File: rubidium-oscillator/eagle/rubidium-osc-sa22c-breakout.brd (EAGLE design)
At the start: 58.9 x 66 mm, 12 parts, among them J1 OSC_TMMH-109-01-G-DV-ES-A, Q1 ZXMP10A13F, Q2 ZXMP10A13F, X1 MKDSN4, X2 MPT9, X3 SMA-142-0701-801/806, X4 SMA-142-0701-801/806, X5 SMA-142-0701-801/806

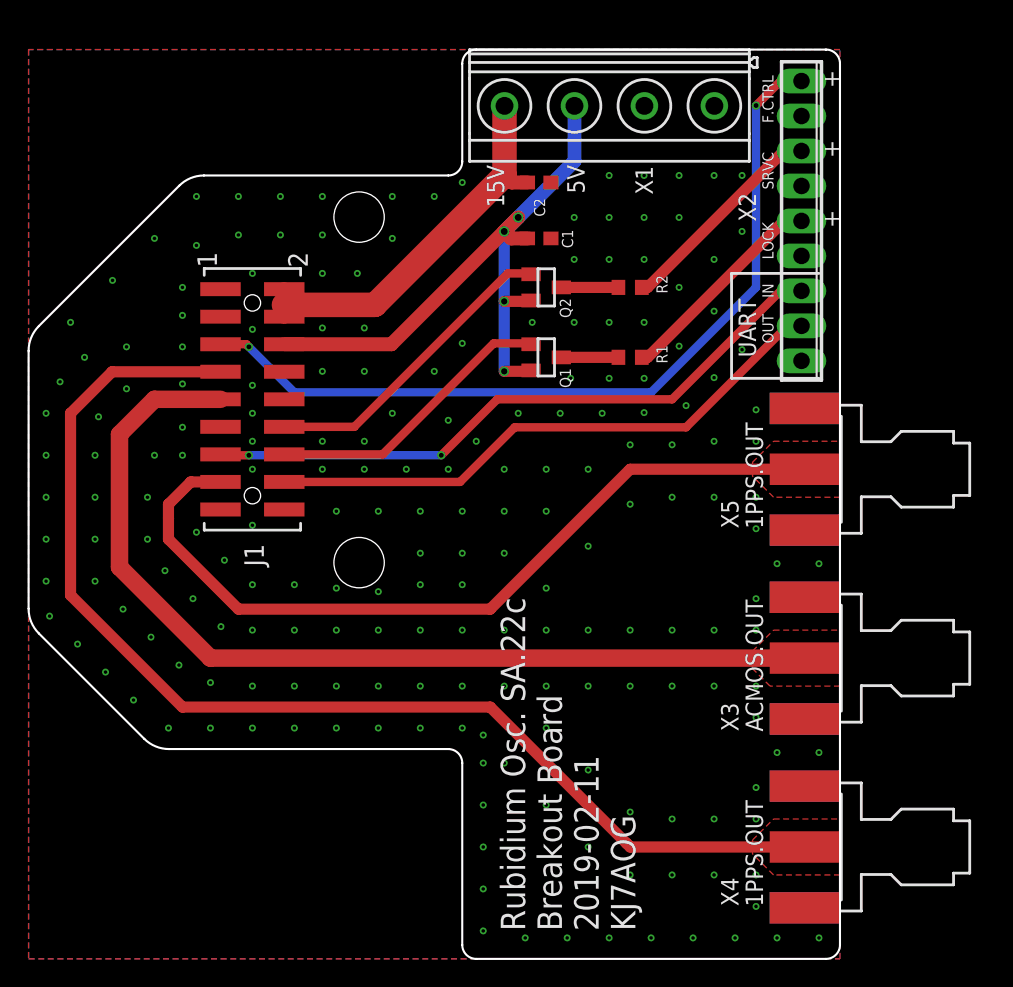
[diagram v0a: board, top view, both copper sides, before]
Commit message: Adjust for proper Phoenix conn sizes.
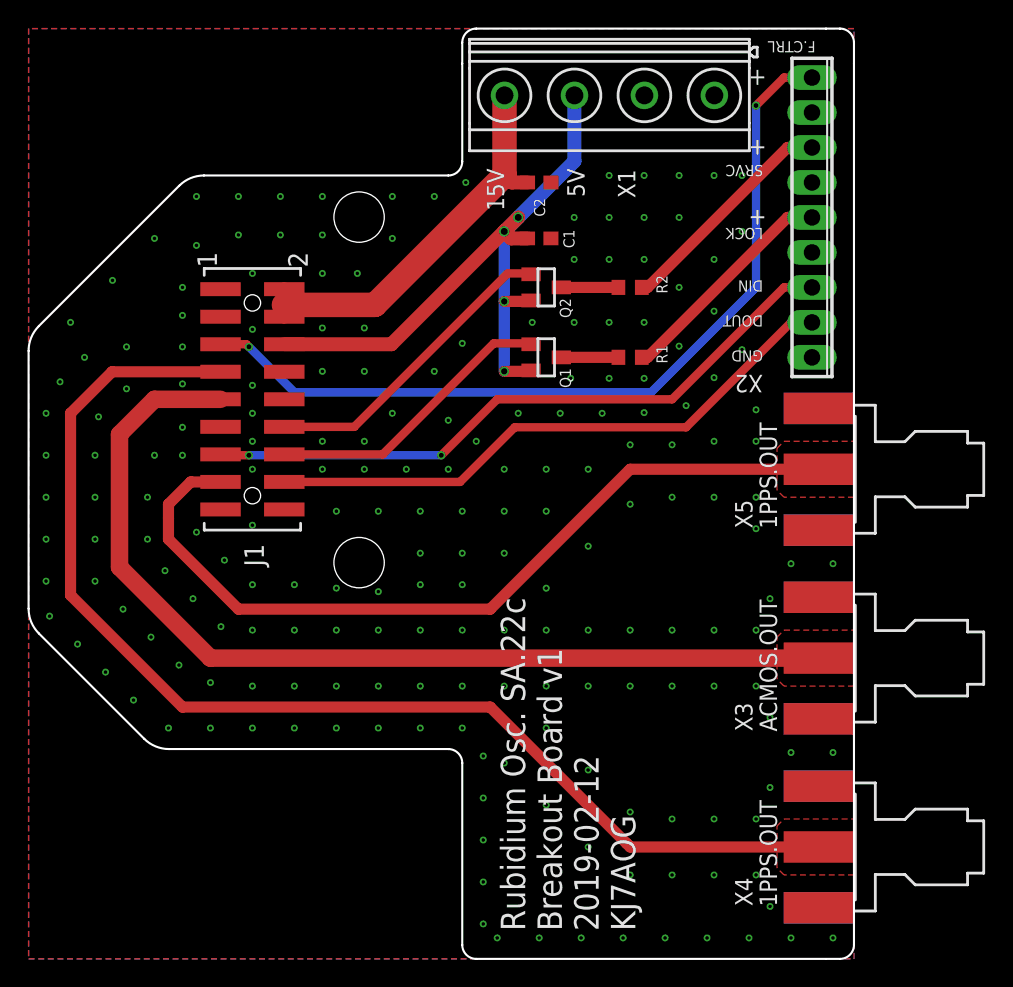
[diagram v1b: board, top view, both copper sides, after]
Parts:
- moved X3 1.02 mm to (59.9, 21.8)
- moved X4 1.02 mm to (59.9, 8.13)
- moved X5 1.02 mm to (59.9, 35.6)
- moved X2 0.80 mm to (56.9, 53.8)
- moved X1 0.76 mm to (42.2, 62.7)
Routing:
- net N$3: track 59.5 -> 60.5 mm
- net N$2: track 86.2 -> 87.3 mm
- net N$1: track 70.5 -> 71.6 mm
- net N$7: track 60.7 -> 61.6 mm
- net N$5: track 42.3 -> 43.1 mm
- net N$4: track 47.2 -> 48.0 mm
- net N$13: track 15.7 -> 16.6 mm
- net N$12: track 15.7 -> 16.6 mm
- net +5V: track 48.0 -> 48.8 mm
- net +15V: track 28.9 -> 29.6 mm
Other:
- board size 58.9 x 66 mm -> 59.9 x 67.6 mm
- board text added: "DIN"
- board text added: "DOUT"
- board text added: "GND"
- board text added: "Rubidium Osc. SA.22c Breakout Board v1 2019-02-12 KJ7AOG"
- board text removed: "IN"
- board text removed: "OUT"
- board text removed: "Rubidium Osc. SA.22c Breakout Board 2019-02-11 KJ7AOG"
- board text removed: "UART"

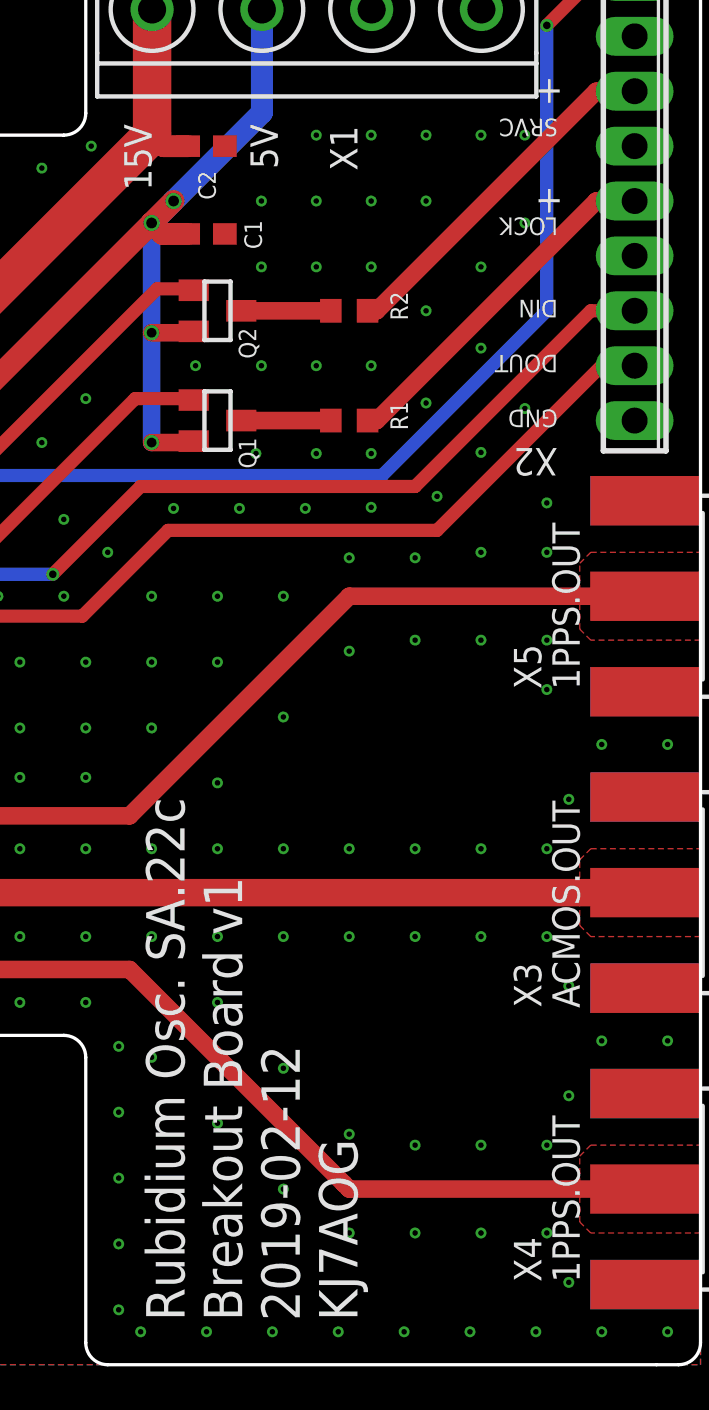
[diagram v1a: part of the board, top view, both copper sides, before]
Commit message: Update vias to tented and moved some, change R1 and R2 for 10mA LEDs
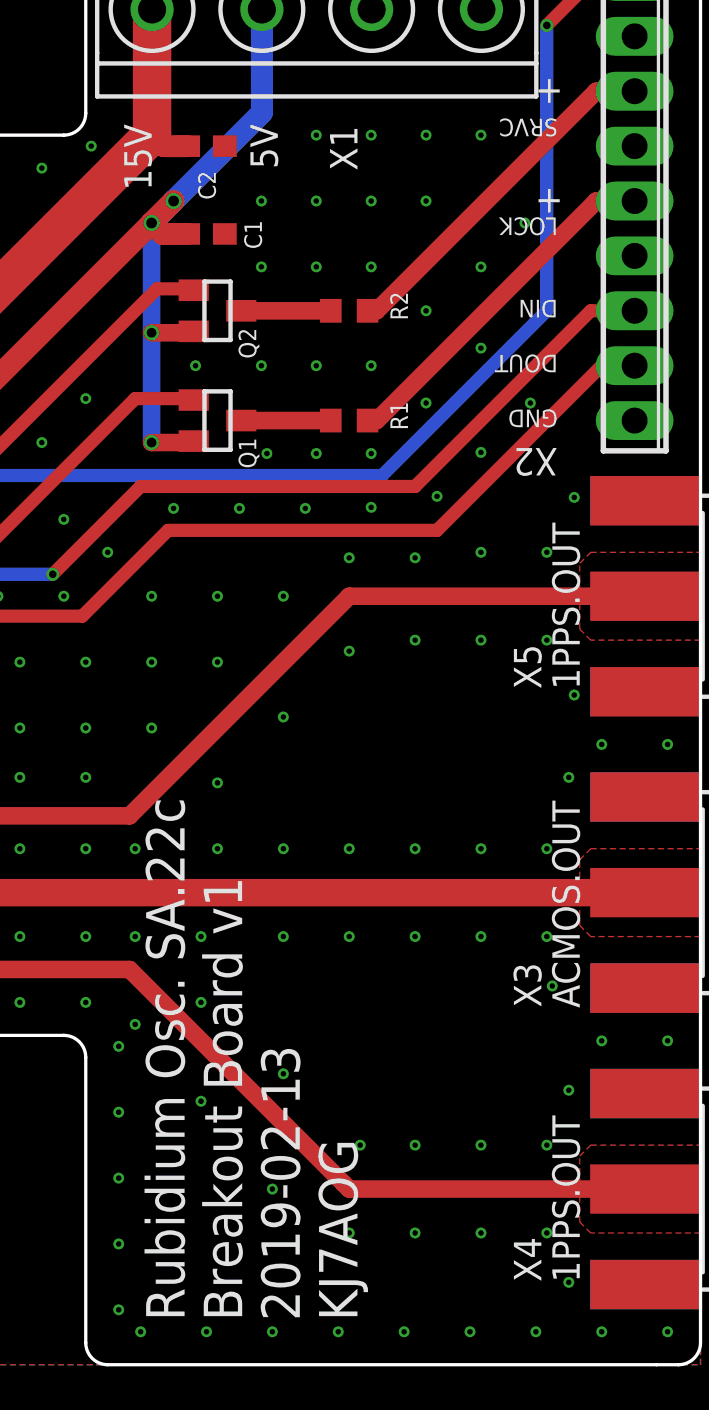
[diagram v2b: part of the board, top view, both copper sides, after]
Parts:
- R1: value 560 -> 270
- R2: value 1k -> 270
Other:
- board text added: "Rubidium Osc. SA.22c Breakout Board v1 2019-02-13 KJ7AOG"
- board text removed: "Rubidium Osc. SA.22c Breakout Board v1 2019-02-12 KJ7AOG"
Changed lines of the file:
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@@
 <layer number="27" name="tValues" color="7" fill="1" visible="yes" active="yes"/>
 <layer number="28" name="bValues" color="7" fill="1" visible="yes" active="yes"/>
-<layer number="29" name="tStop" color="7" fill="3" visible="no" active="yes"/>
+<layer number="29" name="tStop" color="7" fill="3" visible="yes" active="yes"/>
 <layer number="30" name="bStop" color="7" fill="6" visible="no" active="yes"/>
 <layer number="31" name="tCream" color="7" fill="4" visible="no" active="yes"/>
@@
 <text x="34.29" y="2.032" size="1.778" layer="21" ratio="10" rot="R90" align="top-left">Rubidium Osc. SA.22c
 Breakout Board v1
-2019-02-12
+2019-02-13
 KJ7AOG</text>
 <wire x1="53.848" y1="65.024" x2="59.944" y2="65.024" width="0.1524" layer="51"/>
@@
 </class>
 </classes>
-<designrules name="oshpark-2layer">
+<designrules name="oshpark-2layer-tented">
 <description language="en">&lt;b&gt;OSH Park Design Rules&lt;/b&gt;
 &lt;p&gt;
 Please make sure your boards conform to these design rules.
+&lt;/p&gt;
+&lt;p&gt;
+This DRC tents small vias, making them inaccessible on the produced board. This is great for dense routing, BGA, or production boards.
 &lt;/p&gt;
 &lt;p&gt;
@@
 <param name="mlMinCreamFrame" value="0mil"/>
 <param name="mlMaxCreamFrame" value="0mil"/>
-<param name="mlViaStopLimit" value="0mil"/>
+<param name="mlViaStopLimit" value="20mil"/>
 <param name="srRoundness" value="0"/>
 <param name="srMinRoundness" value="0mil"/>
@@
 <attribute name="NAME" x="38.576" y="47.978" size="0.8128" layer="25" rot="R270"/>
 </element>
-<element name="R1" library="rcl" library_urn="urn:adsk.eagle:library:334" package="R0603" package3d_urn="urn:adsk.eagle:package:23555/3" value="560" x="43.688" y="43.688" smashed="yes" rot="R180">
+<element name="R1" library="rcl" library_urn="urn:adsk.eagle:library:334" package="R0603" package3d_urn="urn:adsk.eagle:package:23555/3" value="270" x="43.688" y="43.688" smashed="yes" rot="R180">
 <attribute name="NAME" x="45.593" y="44.577" size="0.8128" layer="25" rot="R270"/>
 <attribute name="SPICEPREFIX" value="R" x="20.828" y="122.428" size="1.778" layer="27" rot="R180" display="off"/>
 </element>
-<element name="R2" library="rcl" library_urn="urn:adsk.eagle:library:334" package="R0603" package3d_urn="urn:adsk.eagle:package:23555/3" value="1k" x="43.688" y="48.768" smashed="yes" rot="R180">
+<element name="R2" library="rcl" library_urn="urn:adsk.eagle:library:334" package="R0603" package3d_urn="urn:adsk.eagle:package:23555/3" value="270" x="43.688" y="48.768" smashed="yes" rot="R180">
 <attribute name="NAME" x="45.593" y="49.657" size="0.8128" layer="25" rot="R270"/>
 <attribute name="SPICEPREFIX" value="R" x="17.018" y="127.508" size="1.778" layer="27" rot="R180" display="off"/>
@@
 <via x="47.244" y="48.768" extent="1-16" drill="0.254"/>
 <via x="49.784" y="50.8" extent="1-16" drill="0.254"/>
-<via x="39.37" y="42.164" extent="1-16" drill="0.254"/>
+<via x="39.878" y="42.164" extent="1-16" drill="0.254"/>
 <via x="42.164" y="42.164" extent="1-16" drill="0.254"/>
 <via x="44.704" y="42.164" extent="1-16" drill="0.254"/>
 <via x="47.244" y="44.5008" extent="1-16" drill="0.254"/>
 <via x="49.784" y="47.0408" extent="1-16" drill="0.254"/>
-<via x="51.816" y="56.896" extent="1-16" drill="0.254"/>
 <via x="51.816" y="52.832" extent="1-16" drill="0.254"/>
 <via x="49.784" y="42.2148" extent="1-16" drill="0.254"/>
-<via x="51.816" y="44.2468" extent="1-16" drill="0.254"/>
+<via x="52.07" y="44.5008" extent="1-16" drill="0.254"/>
 <via x="47.752" y="40.1828" extent="1-16" drill="0.254"/>
 <via x="44.704" y="39.6748" extent="1-16" drill="0.254"/>
@@
 <via x="27.432" y="35.56" extent="1-16" drill="0.254"/>
 <via x="32.512" y="37.592" extent="1-16" drill="0.254"/>
-<via x="34.544" y="23.876" extent="1-16" drill="0.254"/>
+<via x="33.782" y="23.876" extent="1-16" drill="0.254"/>
 <via x="37.592" y="23.876" extent="1-16" drill="0.254"/>
 <via x="40.64" y="23.876" extent="1-16" drill="0.254"/>
 <via x="43.688" y="23.876" extent="1-16" drill="0.254"/>
 <via x="46.736" y="23.876" extent="1-16" drill="0.254"/>
-<via x="34.544" y="19.812" extent="1-16" drill="0.254"/>
-<via x="37.592" y="19.812" extent="1-16" drill="0.254"/>
+<via x="33.782" y="19.812" extent="1-16" drill="0.254"/>
+<via x="36.83" y="19.812" extent="1-16" drill="0.254"/>
 <via x="40.64" y="19.812" extent="1-16" drill="0.254"/>
 <via x="43.688" y="19.812" extent="1-16" drill="0.254"/>
@@
 <via x="49.784" y="19.812" extent="1-16" drill="0.254"/>
 <via x="49.784" y="23.876" extent="1-16" drill="0.254"/>
-<via x="53.848" y="17.526" extent="1-16" drill="0.254"/>
-<via x="53.848" y="26.162" extent="1-16" drill="0.254"/>
+<via x="53.086" y="17.526" extent="1-16" drill="0.254"/>
+<via x="53.848" y="27.178" extent="1-16" drill="0.254"/>
 <via x="52.832" y="23.876" extent="1-16" drill="0.254"/>
 <via x="52.832" y="19.812" extent="1-16" drill="0.254"/>
-<via x="53.848" y="12.446" extent="1-16" drill="0.254"/>
+<via x="53.848" y="12.7" extent="1-16" drill="0.254"/>
 <via x="53.848" y="3.81" extent="1-16" drill="0.254"/>
 <via x="52.832" y="10.16" extent="1-16" drill="0.254"/>
@@
 <via x="49.784" y="10.16" extent="1-16" drill="0.254"/>
 <via x="49.784" y="6.096" extent="1-16" drill="0.254"/>
-<via x="52.832" y="31.242" extent="1-16" drill="0.254"/>
+<via x="54.102" y="30.988" extent="1-16" drill="0.254"/>
 <via x="52.832" y="33.528" extent="1-16" drill="0.254"/>
 <via x="52.832" y="37.592" extent="1-16" drill="0.254"/>
-<via x="52.832" y="39.878" extent="1-16" drill="0.254"/>
+<via x="54.102" y="40.132" extent="1-16" drill="0.254"/>
 <via x="49.784" y="37.592" extent="1-16" drill="0.254"/>
 <via x="49.784" y="33.528" extent="1-16" drill="0.254"/>
@@
 <via x="46.736" y="6.096" extent="1-16" drill="0.254"/>
 <via x="43.688" y="6.096" extent="1-16" drill="0.254"/>
-<via x="43.688" y="10.668" extent="1-16" drill="0.254"/>
-<via x="40.64" y="13.716" extent="1-16" drill="0.254"/>
-<via x="37.592" y="16.764" extent="1-16" drill="0.254"/>
-<via x="40.64" y="8.128" extent="1-16" drill="0.254"/>
-<via x="37.592" y="11.176" extent="1-16" drill="0.254"/>
-<via x="34.544" y="14.224" extent="1-16" drill="0.254"/>
+<via x="44.196" y="10.16" extent="1-16" drill="0.254"/>
+<via x="40.64" y="13.462" extent="1-16" drill="0.254"/>
+<via x="36.83" y="16.764" extent="1-16" drill="0.254"/>
+<via x="40.132" y="8.128" extent="1-16" drill="0.254"/>
+<via x="36.83" y="12.192" extent="1-16" drill="0.254"/>
+<via x="33.782" y="15.748" extent="1-16" drill="0.254"/>
 <via x="33.02" y="14.732" extent="1-16" drill="0.254"/>
 <via x="33.02" y="11.684" extent="1-16" drill="0.254"/>
